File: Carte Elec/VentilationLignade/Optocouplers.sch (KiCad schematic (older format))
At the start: 35 parts, among them U2 OPTO-TRANSISTOR, U3 OPTO-TRANSISTOR, U4 OPTO-TRANSISTOR, U5 OPTO-TRANSISTOR, U6 OPTO-TRANSISTOR

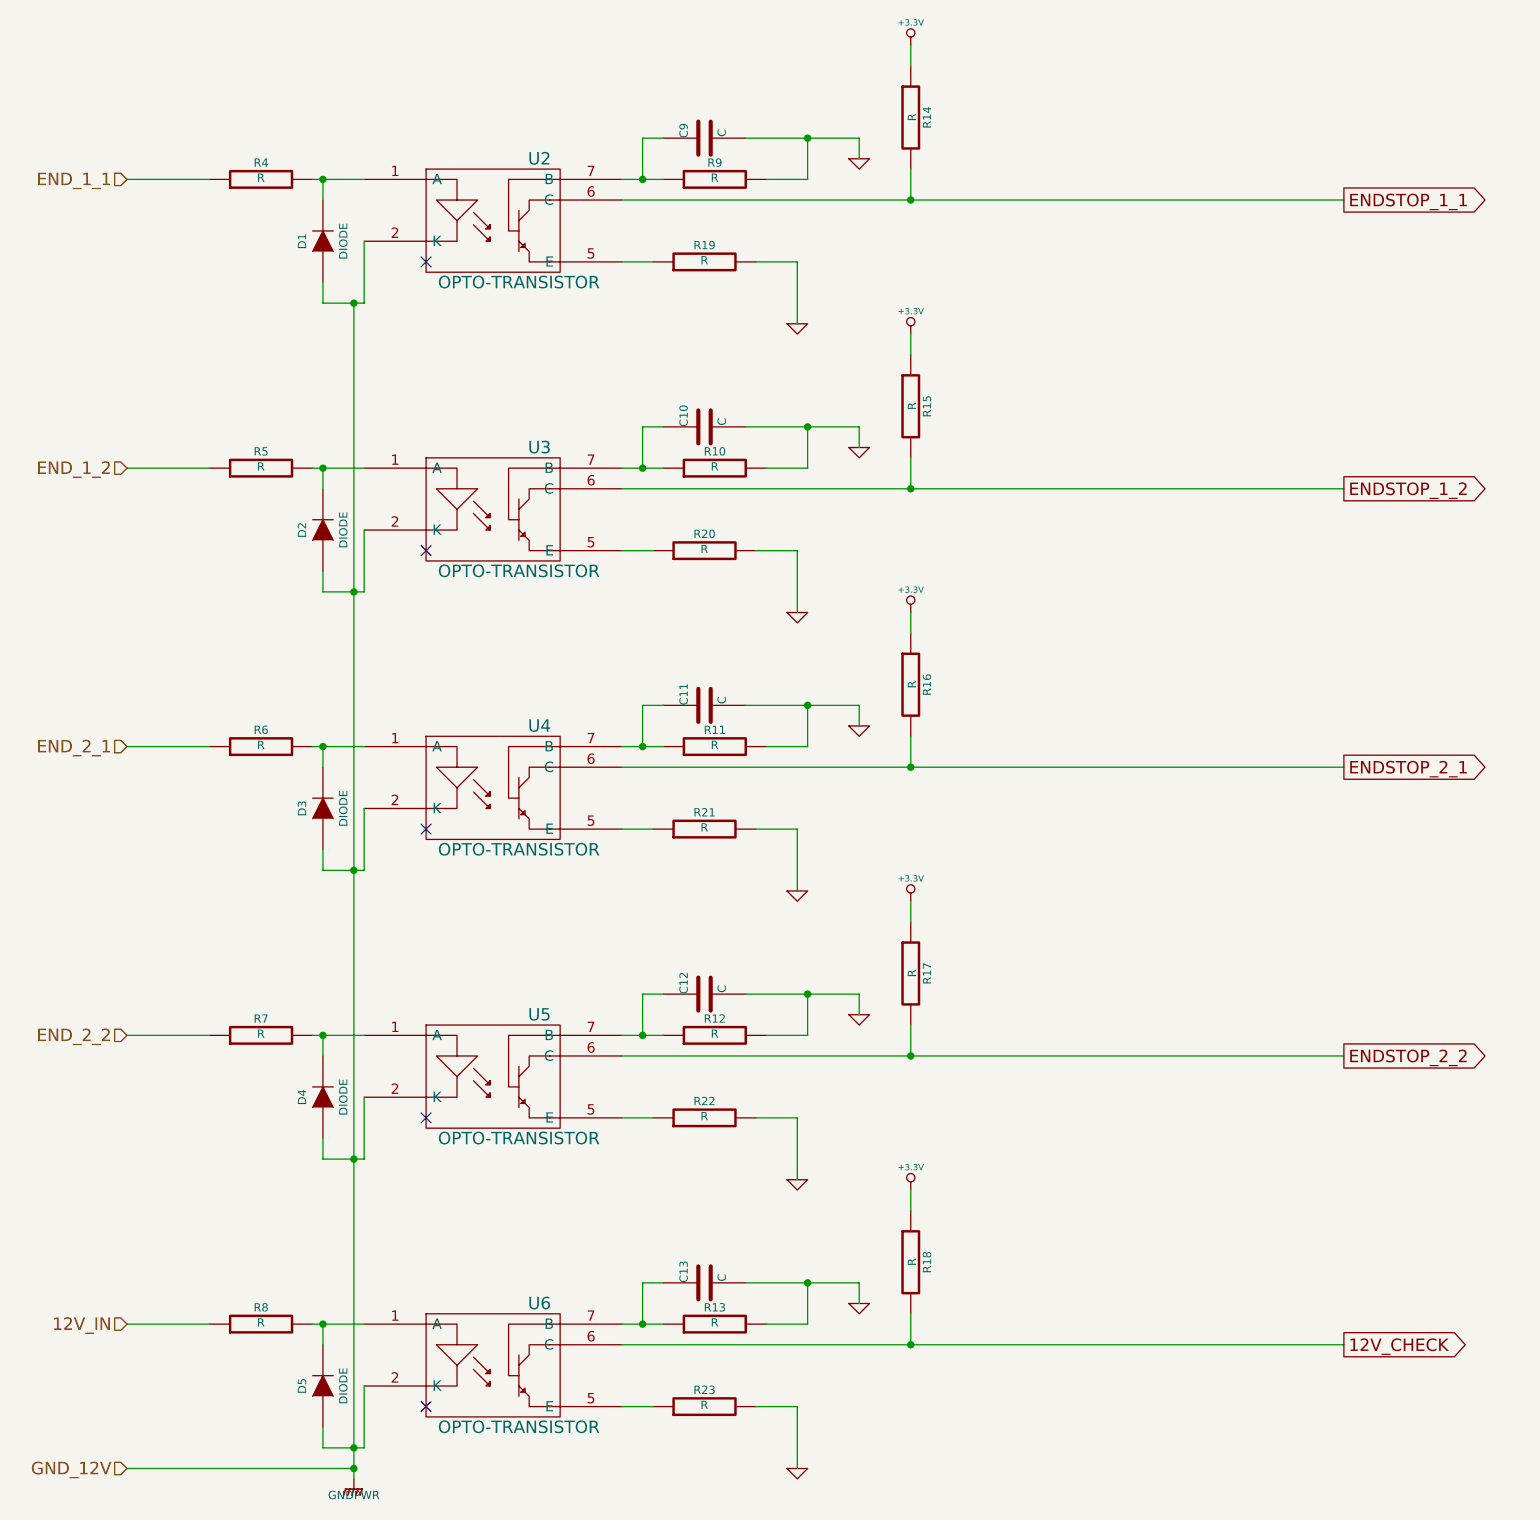
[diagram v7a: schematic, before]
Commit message: Ajout de valeur de composants
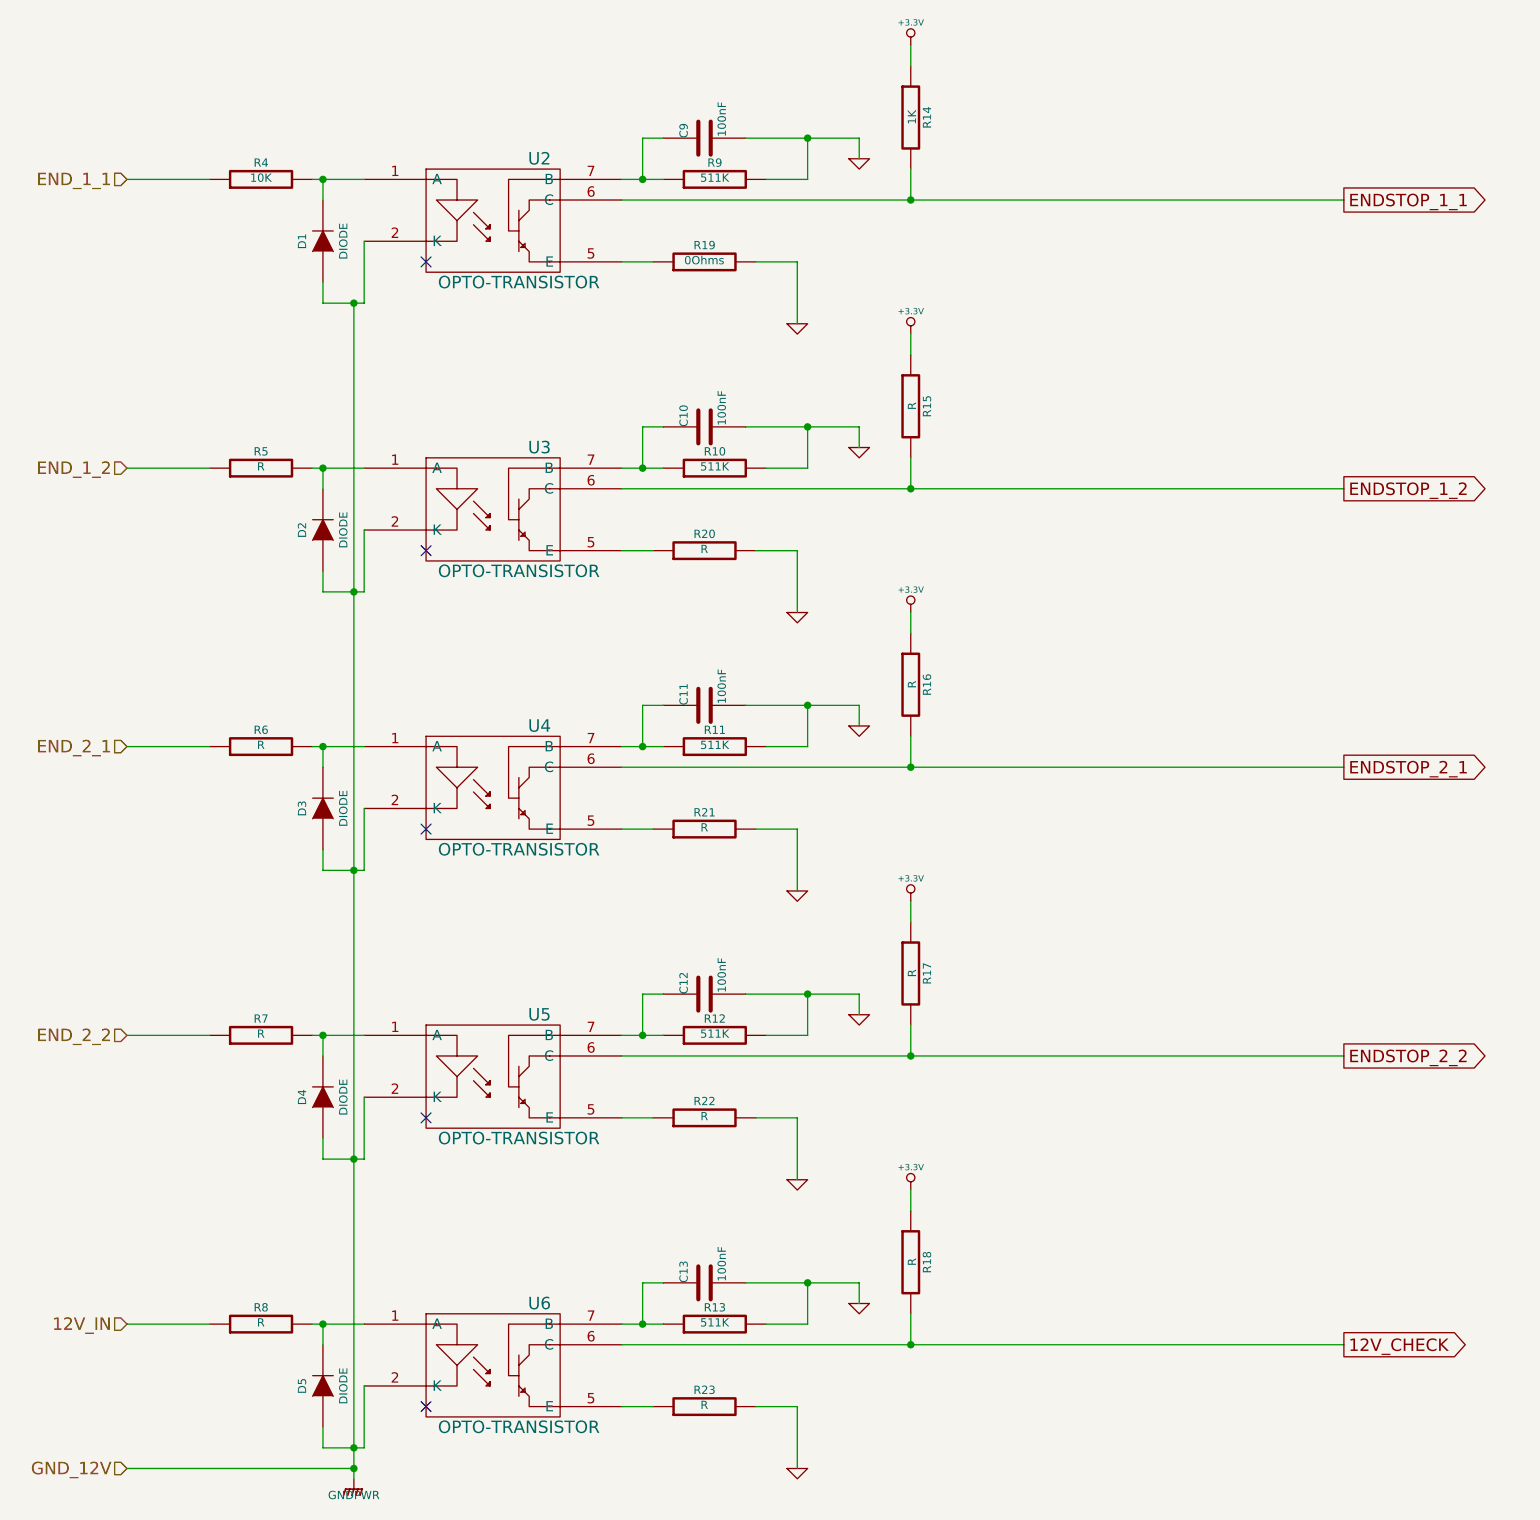
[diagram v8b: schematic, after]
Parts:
- C10, C11, C12, C13, C9: value C -> 100nF
- R10, R11, R12, R13, R9: value R -> 511K
- R14: value R -> 1K
- R19: value R -> 0Ohms
- R4: value R -> 10K
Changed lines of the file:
@@
 AR Path="/55ECC0F8/55F3F577" Ref="R4"  Part="1"
 F 0 "R4" V 2130 1350 40  0000 C CNN
-F 1 "R" V 2057 1351 40  0000 C CNN
+F 1 "10K" V 2057 1351 40  0000 C CNN
 F 2 "Resistors_SMD:R_1206_HandSoldering" V 1980 1350 30  0001 C CNN
 F 3 "~" H 2050 1350 30  0000 C CNN
@@
 AR Path="/55ECC0F8/55F3F5A2" Ref="R9"  Part="1"
 F 0 "R9" V 4330 1350 40  0000 C CNN
-F 1 "R" V 4257 1351 40  0000 C CNN
+F 1 "511K" V 4257 1351 40  0000 C CNN
 F 2 "Resistors_SMD:R_1206_HandSoldering" V 4180 1350 30  0001 C CNN
 F 3 "~" H 4250 1350 30  0000 C CNN
@@
 AR Path="/55ECC0F8/55F3F5B1" Ref="C9"  Part="1"
 F 0 "C9" H 4200 1250 40  0000 L CNN
-F 1 "C" H 4206 1065 40  0000 L CNN
+F 1 "100nF" H 4206 1065 40  0000 L CNN
 F 2 "Capacitors_SMD:C_0805_HandSoldering" H 4238 1000 30  0001 C CNN
 F 3 "~" H 4200 1150 60  0000 C CNN
@@
 AR Path="/55ECC0F8/55F3F61B" Ref="R14"  Part="1"
 F 0 "R14" V 5280 1050 40  0000 C CNN
-F 1 "R" V 5207 1051 40  0000 C CNN
+F 1 "1K" V 5207 1051 40  0000 C CNN
 F 2 "Resistors_SMD:R_1206_HandSoldering" V 5130 1050 30  0001 C CNN
 F 3 "~" H 5200 1050 30  0000 C CNN
@@
 AR Path="/55ECC0F8/55F3F686" Ref="R10"  Part="1"
 F 0 "R10" V 4330 2750 40  0000 C CNN
-F 1 "R" V 4257 2751 40  0000 C CNN
+F 1 "511K" V 4257 2751 40  0000 C CNN
 F 2 "Resistors_SMD:R_1206_HandSoldering" V 4180 2750 30  0001 C CNN
 F 3 "~" H 4250 2750 30  0000 C CNN
@@
 AR Path="/55ECC0F8/55F3F68C" Ref="C10"  Part="1"
 F 0 "C10" H 4200 2650 40  0000 L CNN
-F 1 "C" H 4206 2465 40  0000 L CNN
+F 1 "100nF" H 4206 2465 40  0000 L CNN
 F 2 "Capacitors_SMD:C_0805_HandSoldering" H 4238 2400 30  0001 C CNN
 F 3 "~" H 4200 2550 60  0000 C CNN
@@
 AR Path="/55ECC0F8/55F3F6D3" Ref="R11"  Part="1"
 F 0 "R11" V 4330 4100 40  0000 C CNN
-F 1 "R" V 4257 4101 40  0000 C CNN
+F 1 "511K" V 4257 4101 40  0000 C CNN
 F 2 "Resistors_SMD:R_1206_HandSoldering" V 4180 4100 30  0001 C CNN
 F 3 "~" H 4250 4100 30  0000 C CNN
@@
 AR Path="/55ECC0F8/55F3F6D9" Ref="C11"  Part="1"
 F 0 "C11" H 4200 4000 40  0000 L CNN
-F 1 "C" H 4206 3815 40  0000 L CNN
+F 1 "100nF" H 4206 3815 40  0000 L CNN
 F 2 "Capacitors_SMD:C_0805_HandSoldering" H 4238 3750 30  0001 C CNN
 F 3 "~" H 4200 3900 60  0000 C CNN
@@
 AR Path="/55ECC0F8/55F3F720" Ref="R12"  Part="1"
 F 0 "R12" V 4330 5500 40  0000 C CNN
-F 1 "R" V 4257 5501 40  0000 C CNN
+F 1 "511K" V 4257 5501 40  0000 C CNN
 F 2 "Resistors_SMD:R_1206_HandSoldering" V 4180 5500 30  0001 C CNN
 F 3 "~" H 4250 5500 30  0000 C CNN
@@
 AR Path="/55ECC0F8/55F3F726" Ref="C12"  Part="1"
 F 0 "C12" H 4200 5400 40  0000 L CNN
-F 1 "C" H 4206 5215 40  0000 L CNN
+F 1 "100nF" H 4206 5215 40  0000 L CNN
 F 2 "Capacitors_SMD:C_0805_HandSoldering" H 4238 5150 30  0001 C CNN
 F 3 "~" H 4200 5300 60  0000 C CNN
@@
 AR Path="/55ECC0F8/55F3F774" Ref="R13"  Part="1"
 F 0 "R13" V 4330 6900 40  0000 C CNN
-F 1 "R" V 4257 6901 40  0000 C CNN
+F 1 "511K" V 4257 6901 40  0000 C CNN
 F 2 "Resistors_SMD:R_1206_HandSoldering" V 4180 6900 30  0001 C CNN
 F 3 "~" H 4250 6900 30  0000 C CNN
@@
 AR Path="/55ECC0F8/55F3F77A" Ref="C13"  Part="1"
 F 0 "C13" H 4200 6800 40  0000 L CNN
-F 1 "C" H 4206 6615 40  0000 L CNN
+F 1 "100nF" H 4206 6615 40  0000 L CNN
 F 2 "Capacitors_SMD:C_0805_HandSoldering" H 4238 6550 30  0001 C CNN
 F 3 "~" H 4200 6700 60  0000 C CNN
@@
 AR Path="/55ECC0F8/55F403F8" Ref="R19"  Part="1"
 F 0 "R19" V 4280 1750 40  0000 C CNN
-F 1 "R" V 4207 1751 40  0000 C CNN
+F 1 "0Ohms" V 4207 1751 40  0000 C CNN
 F 2 "Resistors_SMD:R_1206_HandSoldering" V 4130 1750 30  0001 C CNN
 F 3 "~" H 4200 1750 30  0000 C CNN
